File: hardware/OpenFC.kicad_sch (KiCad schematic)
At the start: 0 parts

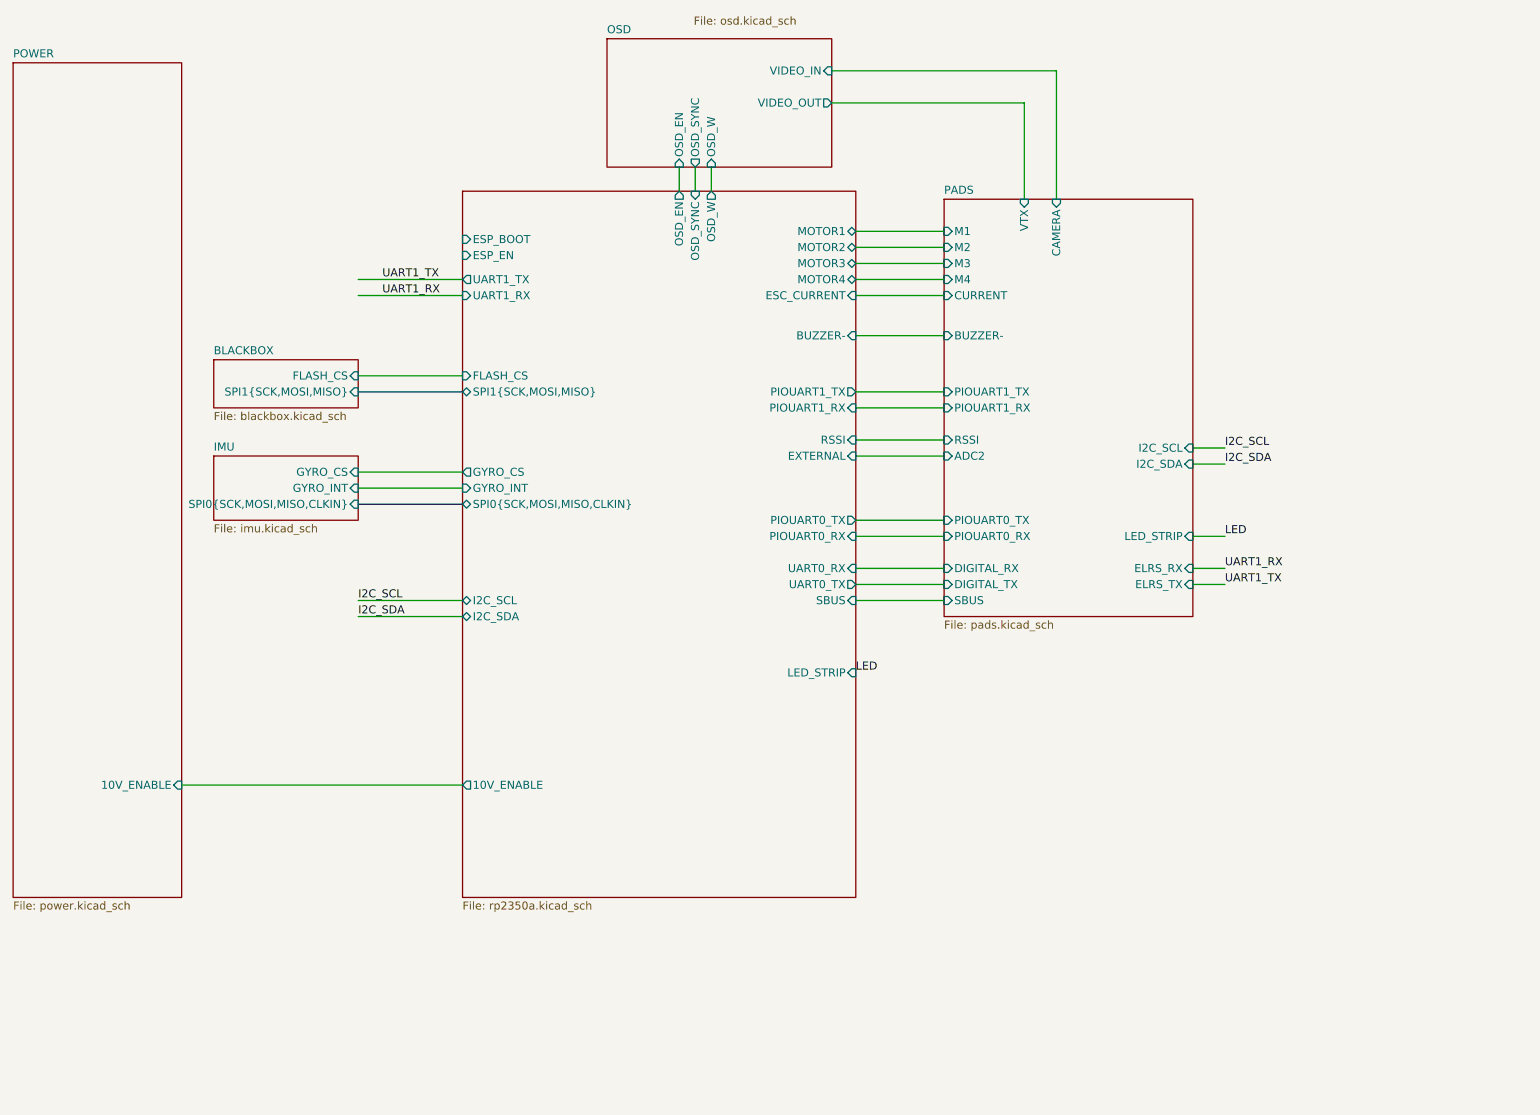
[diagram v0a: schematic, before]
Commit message: Rev 2 (RP2354A): finalize design, update docs, clean repo (#5)
* docs(readme): add analog OSD BOM to Rev 2 change list

Document OSD debugging findings and component changes as a new
Analog OSD section in the Rev 2 Change List:
- HW-12: U19 op-amp TLV9061IDPWR -> COS8051SOT (175MHz video-grade RRIO)
- HW-13: output front-end add AC-couple + DC-restore, power U19 from +5V
- HW-14: U20 comparator TLV3201AIDBVR -> TLV7031DPWR (push-pull, X2SON, ~75% smaller)
- HW-15: add OSD_EN select pull-down (datasheet-required, defaults to pass-through)
- U18 / D9 verified correct, no change; OSD GPIO mapping noted (PA4/5/6)

Also fix HW-11 beeper GPIO: GPIO6 -> GPIO7 (GPIO6 is OSD_SYNC per netlist).

Co-Authored-By: Claude Opus 4.8 (1M context) <noreply@anthropic.com>

* many tiny improvements

- I/O correctness
- SPI0/SPI1/I2C0 bus corrections
- decoupling of DVDD
- ADC_AVDD as per RPi documents
- removal of SBUS
- connect ESC serial
- remove RUN RC-circuit as per RPi documentation
- some more cleanup for readability
- gyro CLKIN decision
- I2C 4.7k pullup

* RP2354A

* piu1

* switch spi

* Update OpenFC.kicad_pcb

* routex2

* some minor tweaks

- remove some unnecessary resistors
- slightly higher 10V rail to account for voltage drop
- some cleanup
- simpler PG 1.8V circuit

* Update imu.kicad_sch

* LED resistors

Also reduced the amount of different resistors for cheaper assembly

* Delete leds.kicad_sch

* remove some unneeded decoupling caps from RP2350

* update MOSFET part numbers

* OSD

* ROUTE

* clean libs

* details

* led names

* Clean routing

* docs: rewrite README + CLAUDE.md for finalized Rev 2 (RP2354A)

Rev 2 is a substantial redesign that the docs no longer matched. Updated
both to the actual schematic, verified from the current netlist:

- MCU: RP2354B (QFN-80, GPIO0-47) -> RP2354A (QFN-60, GPIO0-29). Full GPIO
  map re-derived from the netlist + QFN-60 pinout; all 30 GPIO documented.
- IMU moved to SPI1, microSD to SPI0; ref designators re-annotated
  (op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
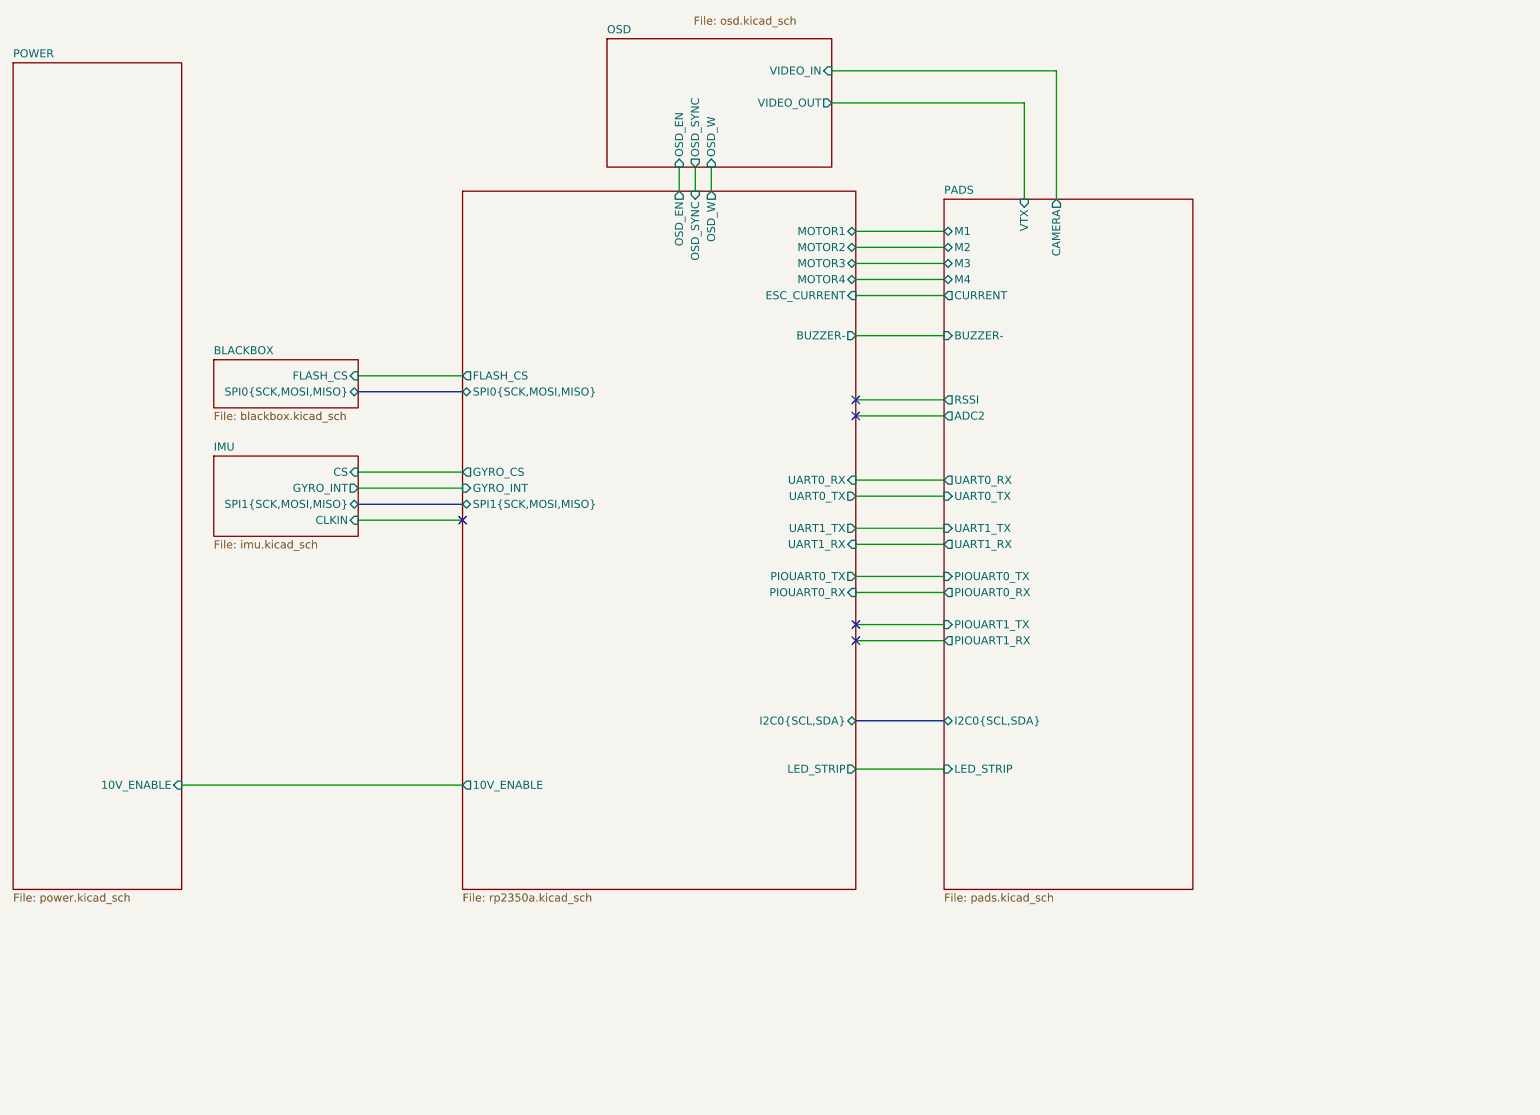
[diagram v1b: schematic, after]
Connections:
- no-connect marks 0 -> 5
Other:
- sheet BLACKBOX ports: added SPI0{SCK,MOSI,MISO}; removed SPI1{SCK,MOSI,MISO}
- sheet IMU ports: added CLKIN, CS, SPI1{SCK,MOSI,MISO}; removed GYRO_CS, SPI0{SCK,MOSI,MISO,CLKIN}
- sheet PADS ports: added I2C0{SCL,SDA}, UART0_RX, UART0_TX, UART1_RX, UART1_TX; removed DIGITAL_RX, DIGITAL_TX, ELRS_RX, ELRS_TX, I2C_SCL, I2C_SDA, SBUS
- sheet RP2350A ports: added I2C0{SCL,SDA}, SPI0{SCK,MOSI,MISO}; removed ESP_BOOT, ESP_EN, EXTERNAL, I2C_SCL, I2C_SDA, PIOUART1_RX, PIOUART1_TX, RSSI, SBUS, SPI0{SCK,MOSI,MISO,CLKIN}

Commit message: docs(schematic): add design annotations to all sheets
Port on-canvas engineering comments from OpenFC-Lite (RP2354B), adapted to the
Mini layout. +41 text items across root, rp2350a, power, imu, osd, blackbox,
pads. Annotation/text only — no net or connectivity changes. Mirrors
hardware/DESIGN_NOTES.md.

Co-Authored-By: Claude Opus 4.8 (1M context) <noreply@anthropic.com>
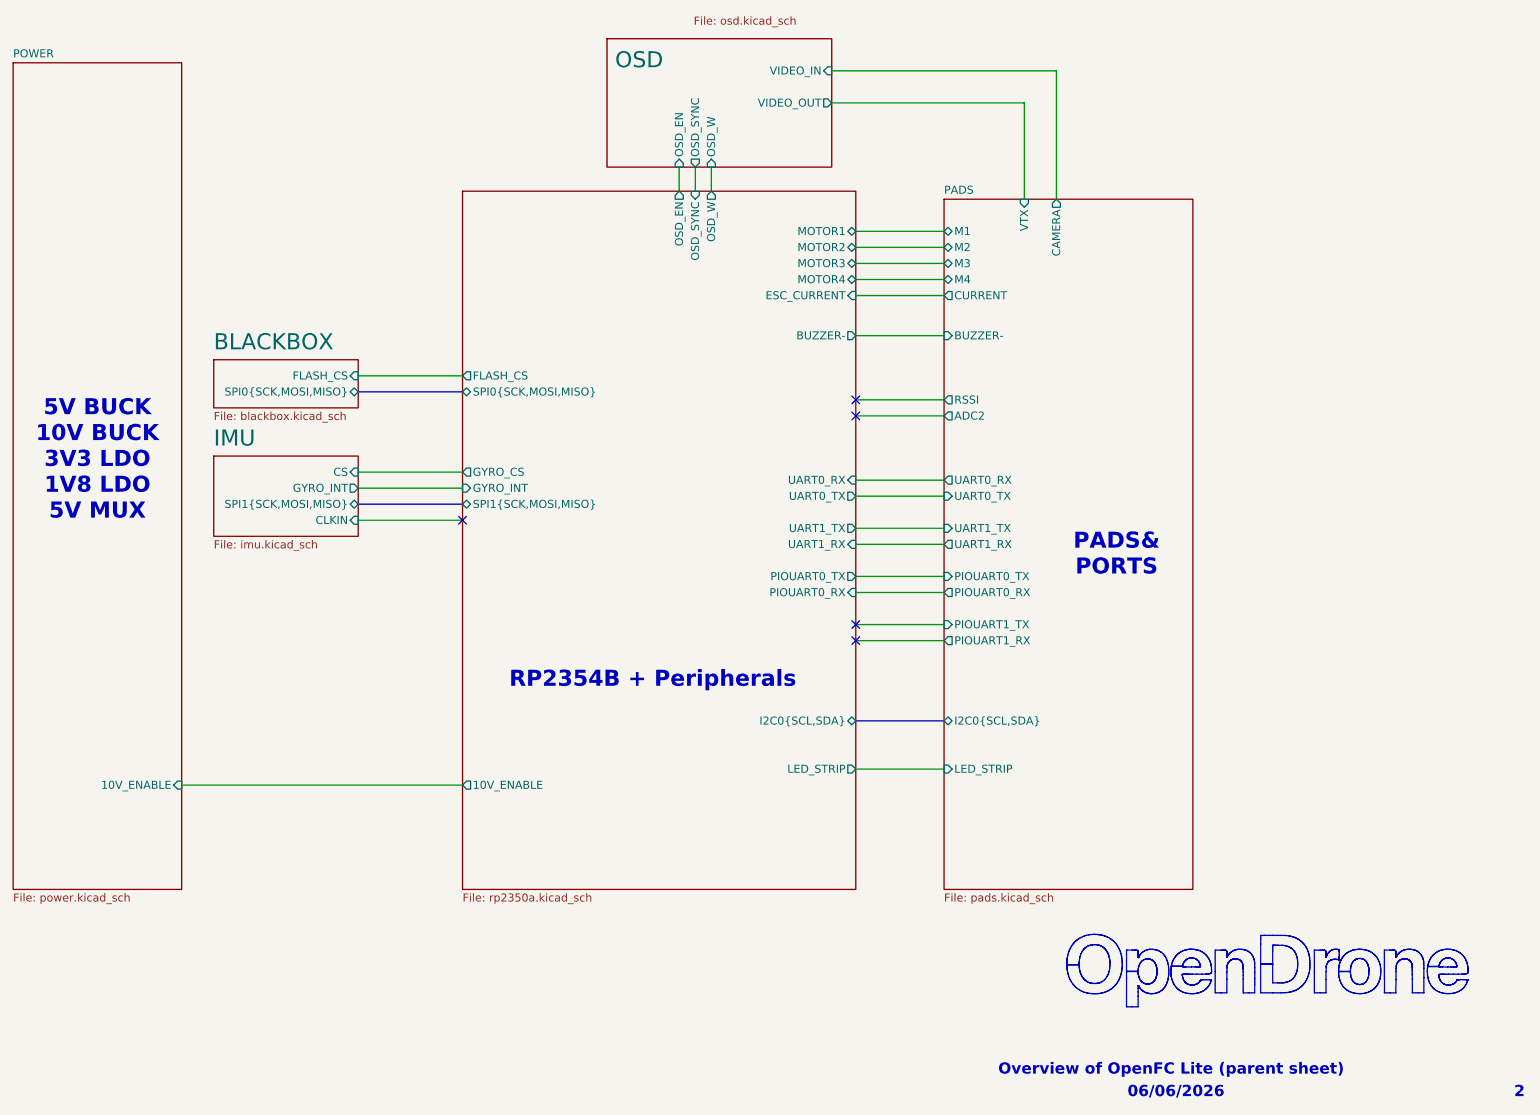
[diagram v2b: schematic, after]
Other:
- note added: "06/06/2026"
- note added: "2"
- note added: "5V BUCK 10V BUCK 3V3 LDO 1V8 LDO 5V MUX"
- note added: "Overview of OpenFC Lite (parent sheet)"
- note added: "PADS& PORTS"
- note added: "RP2354B + Peripherals"

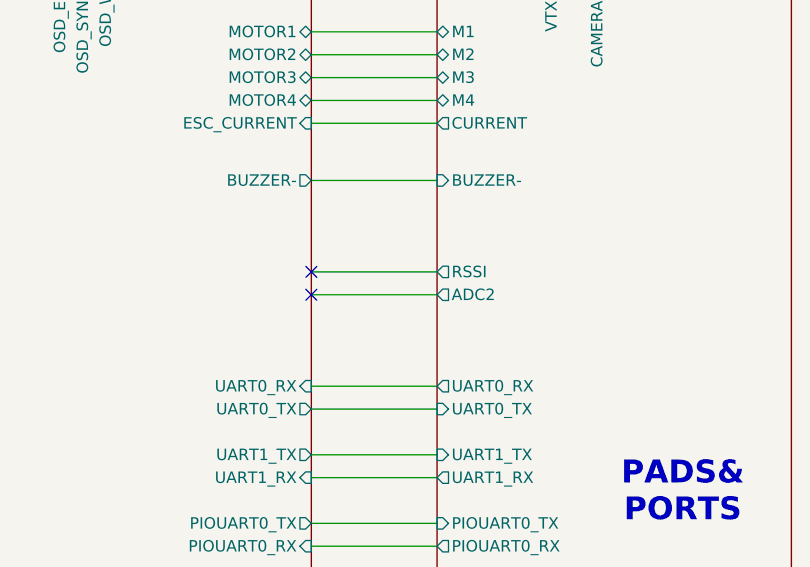
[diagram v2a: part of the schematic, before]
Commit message: Remove RSSI/ADC2 pads that were never on the board
Stan's pads.kicad_sch cleanup deleted the RSSI and ADC2 solder pads
(never fitted on any built board); this completes it on the root sheet:
the two sheet pins, their parked no-connect flags and the two orphan
wires are removed. ERC hier_label_mismatch and no_connect_dangling now
zero; unconnected_wire_endpoint stays at its baseline 3.

Co-Authored-By: Claude Fable 5 <noreply@anthropic.com>
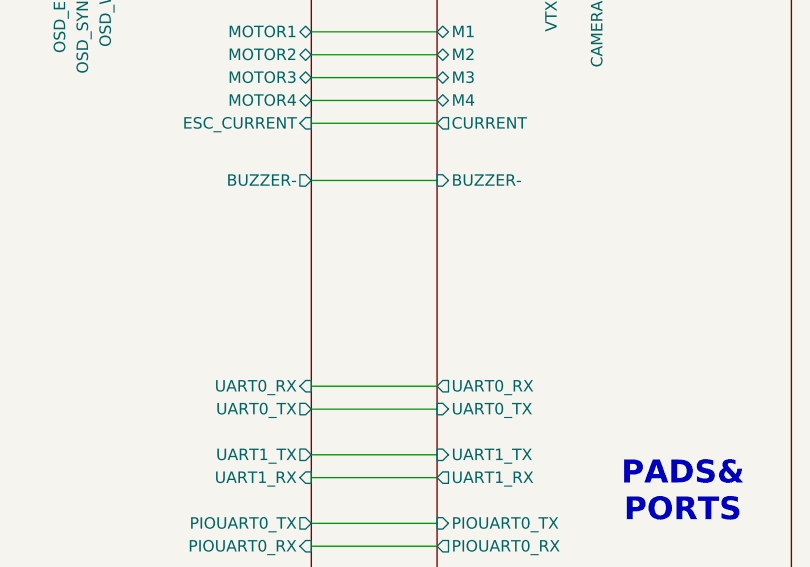
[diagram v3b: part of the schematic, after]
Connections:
- no-connect marks 5 -> 3
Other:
- sheet PADS ports: added none; removed ADC2, RSSI
